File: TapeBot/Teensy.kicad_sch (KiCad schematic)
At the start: 5 parts, among them U3 Teensy4.1

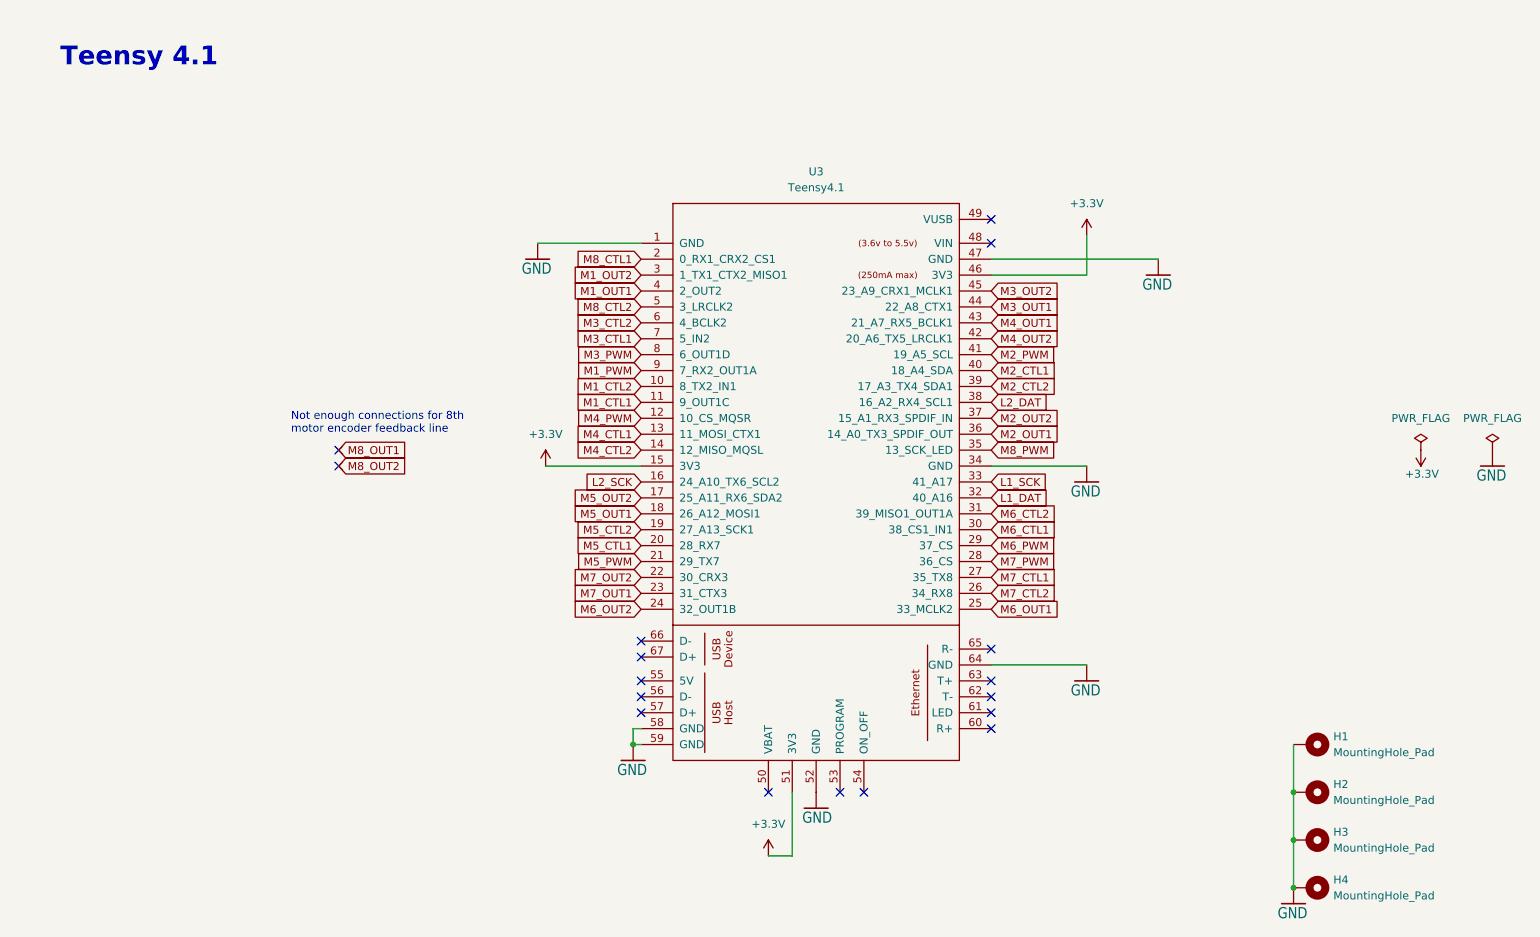
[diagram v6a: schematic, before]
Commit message: First layout of PCB finished
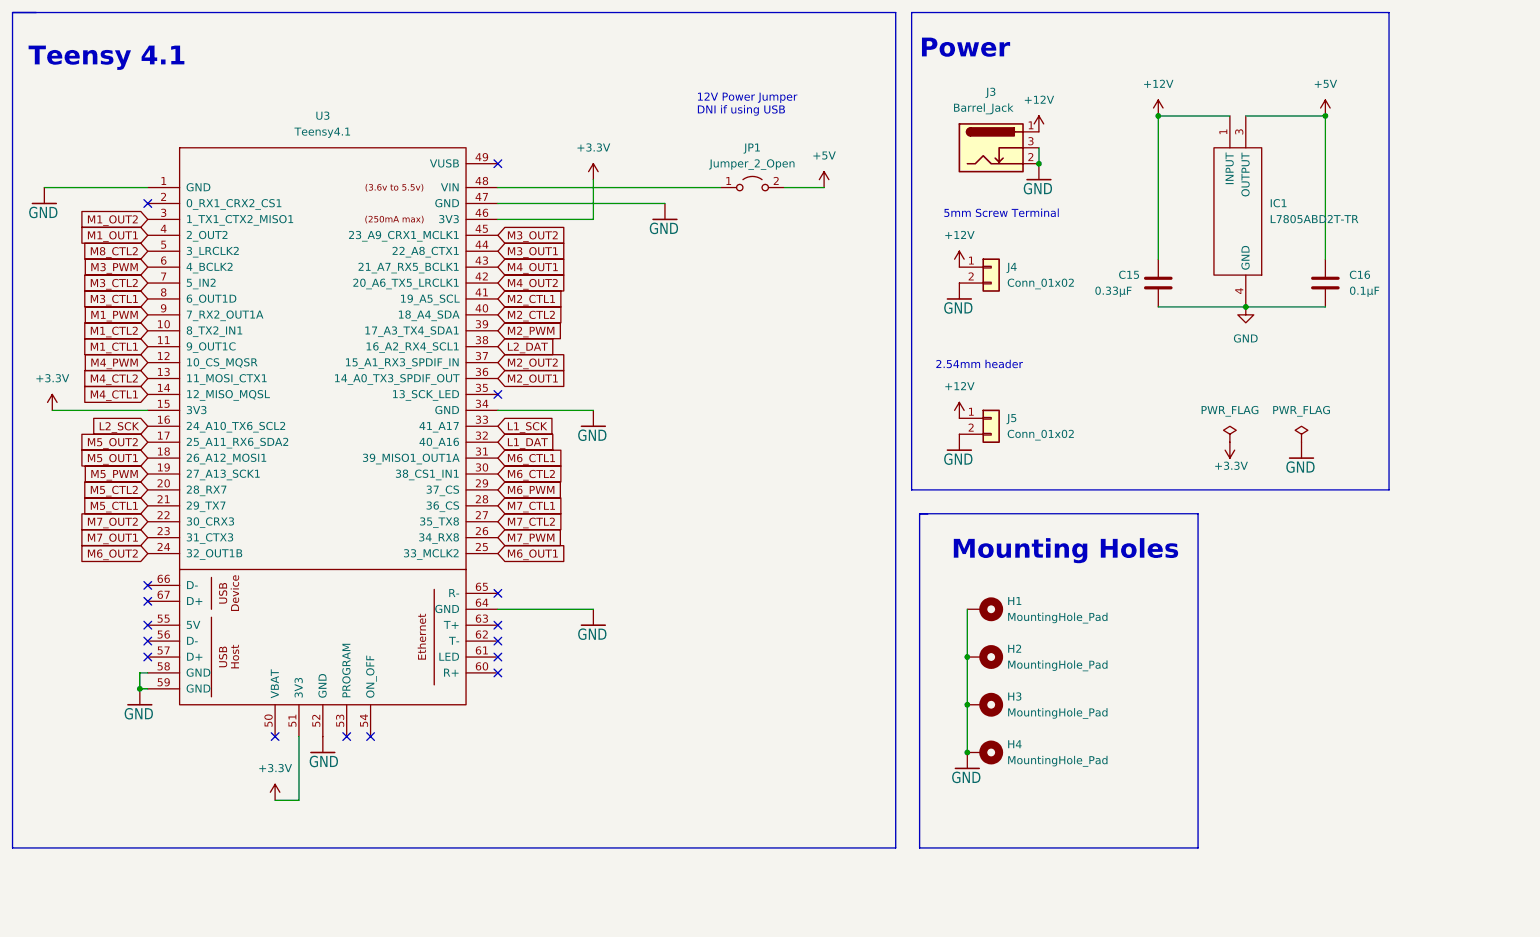
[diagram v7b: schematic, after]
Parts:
- added C15: 0.33µF, Capacitor_SMD:C_0805_2012Metric_Pad1.18x1.45mm_HandSolder, symbol Device:C
- added C16: 0.1µF, Capacitor_SMD:C_0805_2012Metric_Pad1.18x1.45mm_HandSolder, symbol Device:C
- added IC1: L7805ABD2T-TR, D2PAK-STB35NF10T4, symbol ValveController:L7805ABD2T-TR
- added J3: Barrel_Jack, Connector_BarrelJack:BarrelJack_GCT_DCJ200-10-A_Horizontal, symbol Connector:Barrel_Jack_Switch
- added J4: Conn_01x02, tapebot:TE_282837-2, symbol Connector_Generic:Conn_01x02
- added J5: Conn_01x02, Connector_PinHeader_2.54mm:PinHeader_1x02_P2.54mm_Vertical, symbol Connector_Generic:Conn_01x02
- added JP1: Jumper_2_Open, Connector_PinHeader_2.54mm:PinHeader_1x02_P2.54mm_Vertical, symbol Jumper:Jumper_2_Open
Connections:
- net GND: now also C15.2, C16.2, IC1.4 (GND), J3.2, J3.3, J4.2 (Pin_2), J5.2 (Pin_2)
- net M2_CTL1: now also U3.41 (19_A5_SCL); no longer U3.40 (18_A4_SDA)
- net M2_CTL2: now also U3.40 (18_A4_SDA); no longer U3.39 (17_A3_TX4_SDA1)
- net M2_PWM: now also U3.39 (17_A3_TX4_SDA1); no longer U3.41 (19_A5_SCL)
- net M3_CTL1: now also U3.8 (6_OUT1D); no longer U3.7 (5_IN2)
- net M3_CTL2: now also U3.7 (5_IN2); no longer U3.6 (4_BCLK2)
- net M3_PWM: now also U3.6 (4_BCLK2); no longer U3.8 (6_OUT1D)
- net M4_CTL1: now also U3.14 (12_MISO_MQSL); no longer U3.13 (11_MOSI_CTX1)
- net M4_CTL2: now also U3.13 (11_MOSI_CTX1); no longer U3.14 (12_MISO_MQSL)
- net M5_CTL1: now also U3.21 (29_TX7); no longer U3.20 (28_RX7)
- net M5_CTL2: now also U3.20 (28_RX7); no longer U3.19 (27_A13_SCK1)
- net M5_PWM: now also U3.19 (27_A13_SCK1); no longer U3.21 (29_TX7)
- net M6_CTL1: now also U3.31 (39_MISO1_OUT1A); no longer U3.30 (38_CS1_IN1)
- net M6_CTL2: now also U3.30 (38_CS1_IN1); no longer U3.31 (39_MISO1_OUT1A)
- net M7_CTL1: now also U3.28 (36_CS); no longer U3.27 (35_TX8)
- net M7_CTL2: now also U3.27 (35_TX8); no longer U3.26 (34_RX8)
- net M7_PWM: now also U3.26 (34_RX8); no longer U3.28 (36_CS)
- net at U3.48 (VIN): now also JP1.1 (A)
- net M8_CTL1: no longer names the net of U3.2 (0_RX1_CRX2_CS1)
- net M8_PWM: no longer names the net of U3.35 (13_SCK_LED)
- new net +12V: C15.1, IC1.1 (INPUT), J3.1, J4.1 (Pin_1), J5.1 (Pin_1)
- new net +5V: C16.1, IC1.3 (OUTPUT), JP1.2 (B)
- no-connect marks 17 -> 16
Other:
- note added: "12V Power Jumper DNI if using USB"
- note added: "2.54mm header"
- note added: "5mm Screw Terminal"
- note added: "Mounting Holes"
- note added: "Power"
- note removed: "Not enough connections for 8th motor encoder feedback line"
- moved on the sheet: H1, H2, H3, H4, U3
